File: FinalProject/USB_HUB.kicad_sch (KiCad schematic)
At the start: 42 parts, among them U12 TUSB8041, U2 TPS2561DRCR, Y1 Crystal

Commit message: fix schematic
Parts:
- removed Y1: Crystal, symbol Device:Crystal
- added Y3: ABM3C-24.000MHZ-D4Y-T, CRYSTAL_ABM3C_ABR, symbol 2025-04-27_02-03-10:ABM3C-24.000MHZ-D4Y-T
- FB1, FB2, FB5, FB6: footprint (none) -> Inductor_SMD:L_0603_1608Metric
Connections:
- net GND: now also Y3.2, Y3.4
- net at C67.1, R38.2, U12.61 (XO): now also Y3.3
- net at C68.1, R38.1, U12.62 (XI): now also Y3.1
- net BATEN0: no longer names the net of U12.36 (PWRCTL1/BATEN1)
- net BATEN1: no longer names the net of U12.35 (PWRCTL2/BATEN2)
- net OVERCUR0: no longer names the net of U12.46 (OVERCUR1z)
- net OVERCUR1: no longer names the net of U12.47 (OVERCUR2z)
- no-connect marks 4 -> 8

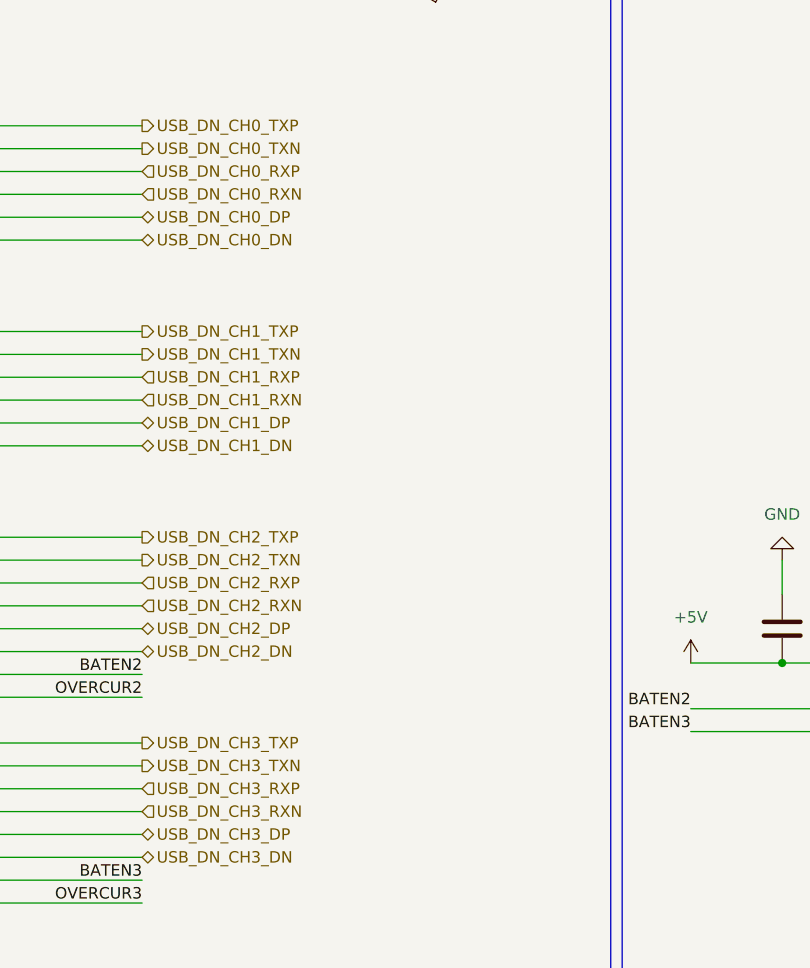
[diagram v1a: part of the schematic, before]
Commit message: fix footprint
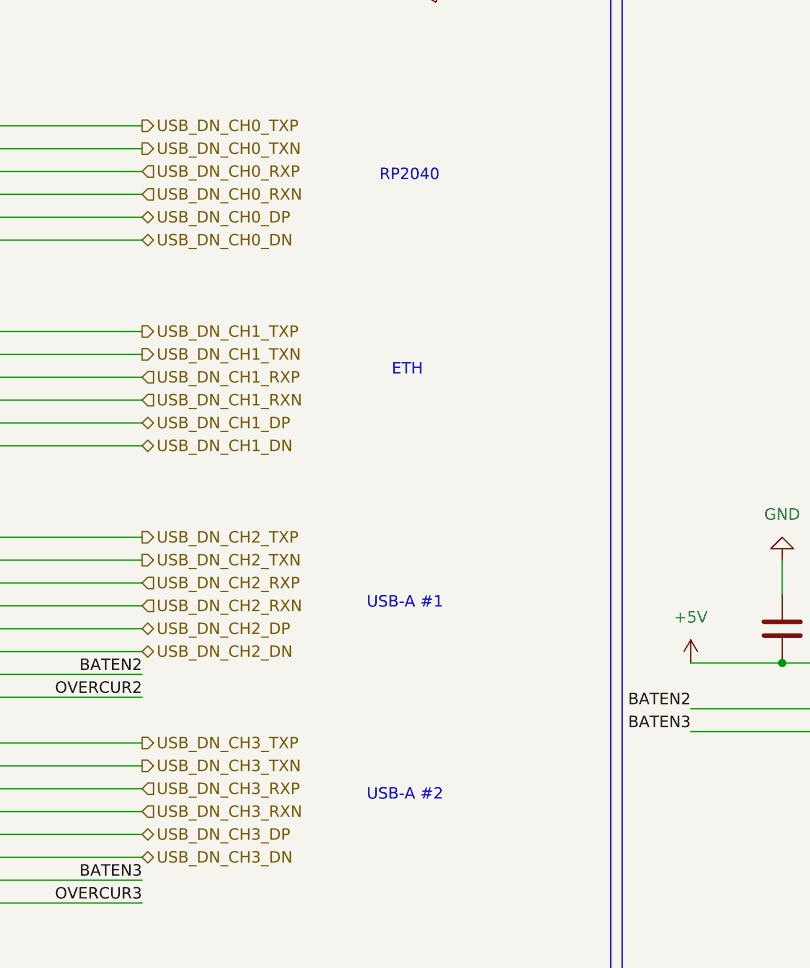
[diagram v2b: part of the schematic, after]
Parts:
- FB1, FB2, FB5, FB6: footprint Inductor_SMD:L_0603_1608Metric -> Inductor_SMD:L_0805_2012Metric
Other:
- note added: "ETH"
- note added: "RP2040"
- note added: "USB-A #1"
- note added: "USB-A #2"
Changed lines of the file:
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@@
 		)
 	)
+	(text "USB-A #1\n"
+		(exclude_from_sim no)
+		(at 201.93 106.426 0)
+		(effects
+			(font
+				(size 1.27 1.27)
+			)
+		)
+	)
+	(text "RP2040\n"
+		(exclude_from_sim no)
+		(at 202.438 58.928 0)
+		(effects
+			(font
+				(size 1.27 1.27)
+			)
+		)
+	)
+	(text "USB-A #2\n"
+		(exclude_from_sim no)
+		(at 201.93 127.762 0)
+		(effects
+			(font
+				(size 1.27 1.27)
+			)
+		)
+	)
+	(text "ETH\n"
+		(exclude_from_sim no)
+		(at 202.184 80.518 0)
+		(effects
+			(font
+				(size 1.27 1.27)
+			)
+		)
+	)
 	(text "Power Switch"
 		(exclude_from_sim no)
@@
 	)
 	(junction
-		(at 109.22 44.45)
+		(at 101.6 45.72)
 		(diameter 0)
 		(color 0 0 0 0)
 	)
 	(junction
-		(at 166.37 27.94)
+		(at 109.22 44.45)
 		(diameter 0)
 		(color 0 0 0 0)
 	)
 	(junction
-		(at 62.23 29.21)
+		(at 166.37 27.94)
 		(diameter 0)
 		(color 0 0 0 0)
 	)
 	(junction
-		(at 360.68 123.19)
+		(at 62.23 29.21)
 		(diameter 0)
 		(color 0 0 0 0)
 	)
 	(junction
-		(at 99.06 45.72)
+		(at 360.68 123.19)
 		(diameter 0)
 		(color 0 0 0 0)
@@
 	)
 	(junction
+		(at 99.06 45.72)
+		(diameter 0)
+		(color 0 0 0 0)
+	)
+	(junction
 		(at 78.74 63.5)
 		(diameter 0)
@@
 	)
 	(junction
+		(at 96.52 45.72)
+		(diameter 0)
+		(color 0 0 0 0)
+	)
+	(junction
 		(at 62.23 36.83)
 		(diameter 0)
@@
 	)
 	(junction
-		(at 101.6 45.72)
+		(at 96.52 36.83)
 		(diameter 0)
 		(color 0 0 0 0)
@@
 	)
 	(junction
-		(at 96.52 45.72)
-		(diameter 0)
-		(color 0 0 0 0)
-	)
-	(junction
 		(at 189.23 36.83)
 		(diameter 0)
@@
 	)
 	(junction
-		(at 96.52 36.83)
-		(diameter 0)
-		(color 0 0 0 0)
-	)
-	(junction
 		(at 363.22 113.03)
 		(diameter 0)
@@
 	(wire
 		(pts
+			(xy 96.52 45.72) (xy 99.06 45.72)
+		)
+		(stroke
+			(width 0)
+			(type default)
+		)
+	)
+	(wire
+		(pts
 			(xy 360.68 123.19) (xy 356.87 123.19)
 		)
@@
 	(wire
 		(pts
+			(xy 99.06 45.72) (xy 101.6 45.72)
+		)
+		(stroke
+			(width 0)
+			(type default)
+		)
+	)
+	(wire
+		(pts
 			(xy 152.4 116.84) (xy 172.72 116.84)
 		)
@@
 	(wire
 		(pts
-			(xy 152.4 106.68) (xy 172.72 106.68)
+			(xy 96.52 36.83) (xy 96.52 45.72)
 		)
 		(stroke
@@
 	(wire
 		(pts
-			(xy 99.06 45.72) (xy 101.6 45.72)
+			(xy 152.4 106.68) (xy 172.72 106.68)
 		)
 		(stroke
@@
 	(wire
 		(pts
-			(xy 101.6 45.72) (xy 104.14 45.72)
-		)
-		(stroke
-			(width 0)
-			(type default)
-		)
-	)
-	(wire
-		(pts
 			(xy 127 44.45) (xy 127 45.72)
 		)
@@
 	(wire
 		(pts
-			(xy 96.52 45.72) (xy 99.06 45.72)
-		)
-		(stroke
-			(width 0)
-			(type default)
-		)
-	)
-	(wire
-		(pts
-			(xy 96.52 36.83) (xy 96.52 45.72)
-		)
-		(stroke
-			(width 0)
-			(type default)
-		)
-	)
-	(wire
-		(pts
 			(xy 152.4 78.74) (xy 172.72 78.74)
 		)
@@
 	(wire
 		(pts
+			(xy 101.6 45.72) (xy 104.14 45.72)
+		)
+		(stroke
+			(width 0)
+			(type default)
+		)
+	)
+	(wire
+		(pts
 			(xy 359.41 105.41) (xy 363.22 105.41)
 		)
@@
 			)
 		)
-		(property "Footprint" "Inductor_SMD:L_0603_1608Metric"
+		(property "Footprint" "Inductor_SMD:L_0805_2012Metric"
 			(at 205.74 38.608 90)
 			(effects
@@
 			)
 		)
-		(property "Footprint" "Inductor_SMD:L_0603_1608Metric"
+		(property "Footprint" "Inductor_SMD:L_0805_2012Metric"
 			(at 375.92 117.348 90)
 			(effects
@@
 			)
 		)
-		(property "Footprint" "Inductor_SMD:L_0603_1608Metric"
+		(property "Footprint" "Inductor_SMD:L_0805_2012Metric"
 			(at 38.1 38.608 90)
 			(effects
@@
 			)
 		)
-		(property "Footprint" "Inductor_SMD:L_0603_1608Metric"
+		(property "Footprint" "Inductor_SMD:L_0805_2012Metric"
 			(at 375.92 114.808 90)
 			(effects

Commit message: help
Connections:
- net USB_FB_1.1V: now reaches C22.2, C23.2, C24.2, C25.2, C26.2, C27.2, C28.2, C29.2, FB1.1, U12.13 (VDD), U12.21 (VDD), U12.28 (VDD), U12.31 (VDD), U12.5 (VDD), U12.51 (VDD), U12.57 (VDD), U12.8 (VDD)
- net USB_FB_3.3V: now reaches C30.2, C31.2, C32.2, C33.2, C34.2, FB2.2, U12.16 (VDD33), U12.34 (VDD33), U12.52 (VDD33), U12.63 (VDD33)
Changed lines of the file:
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@@
+		)
+	)
+	(label "USB_FB_1.1V"
+		(at 189.23 36.83 270)
+		(effects
+			(font
+				(size 1.27 1.27)
+			)
+			(justify right bottom)
 		)
 	)
@@
 		(effects
 			(font
+				(size 1.27 1.27)
+			)
+			(justify right bottom)
+		)
+	)
+	(label "USB_FB_3.3V"
+		(at 50.8 36.83 270)
+		(effects
+			(font

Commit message: update big capacitors footprint to use bigger than 0603
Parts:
- C3, C4: footprint Capacitor_SMD:C_0603_1608Metric -> Capacitor_SMD:C_1210_3225Metric
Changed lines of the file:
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@@
 			)
 		)
-		(property "Footprint" "Capacitor_SMD:C_0603_1608Metric"
+		(property "Footprint" "Capacitor_SMD:C_1210_3225Metric"
 			(at 356.87 119.38 0)
 			(effects
@@
 			)
 		)
-		(property "Footprint" "Capacitor_SMD:C_0603_1608Metric"
+		(property "Footprint" "Capacitor_SMD:C_1210_3225Metric"
 			(at 363.22 109.22 0)
 			(effects
